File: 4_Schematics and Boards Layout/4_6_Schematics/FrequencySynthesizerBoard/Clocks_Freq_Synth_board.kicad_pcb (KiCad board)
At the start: 6 copper layers, 100 x 100 mm, 188 parts, among them IC1 AD9523BCPZ, J1 142-0731-211, J10 142-0731-211, J11 142-0731-211, J12 142-0731-211, J13 142-0731-211, J2 142-0731-211, J3 CJT-T-P-HH-ST-TH1, J4 CJT-T-P-HH-ST-TH1, J5 142-0731-211, J6 142-0731-211, J7 142-0731-211, J8 142-0731-211, J9 142-0731-211, U1 ADF4382ABCCZ, U10 ATS1005-3DB-FD-T05, U2 MTX2-143+, U3 MTX2-143+, U4 ATS1005-3DB-FD-T05, U5 ATS1005-3DB-FD-T05, U6 ADF4382ABCCZ, U7 MTX2-143+, U8 ATS1005-3DB-FD-T05, U9 MTX2-143+, X10 22-23-2021, X11 22-23-2021, X12 22-23-2021, X13 22-23-2021, X14 22-23-2021, X15 22-23-2021, X4 ECOC-2522-100.000-3HC, X5 CVHD-950-50.000, X6 CVHD-950-50.000

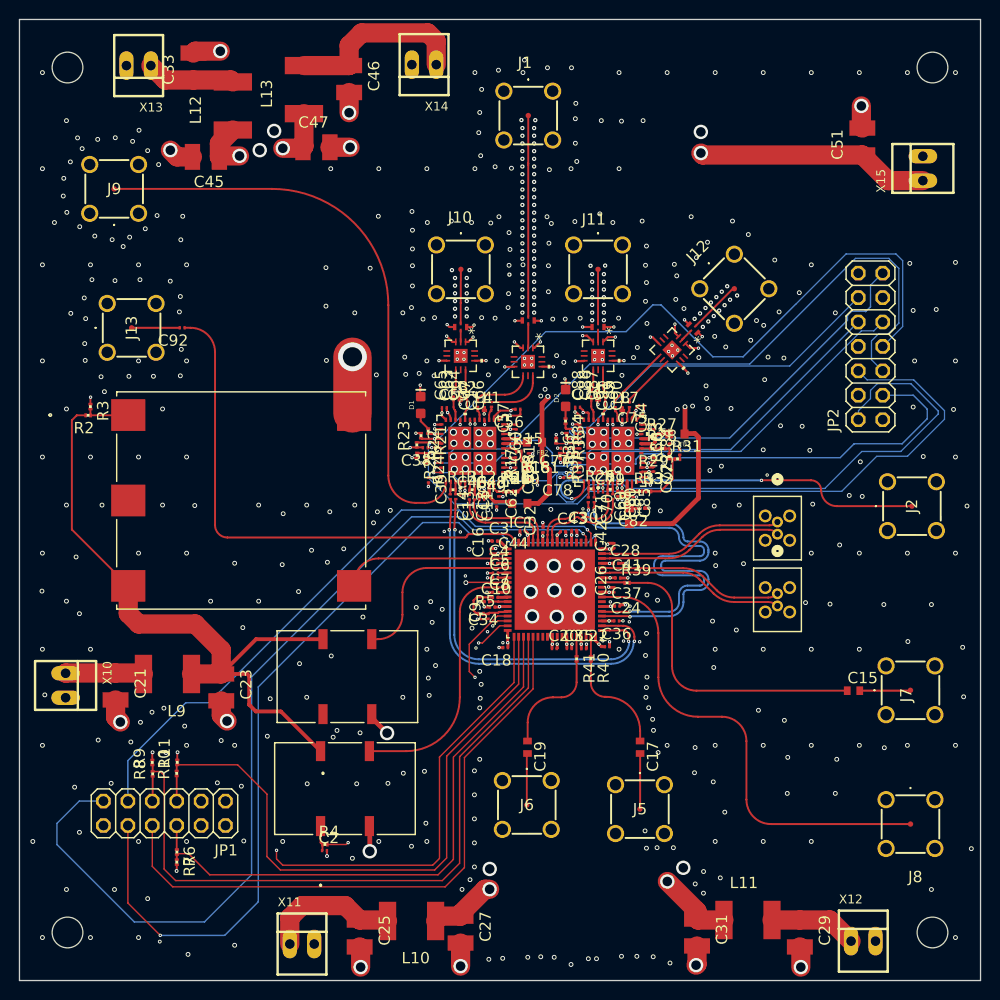
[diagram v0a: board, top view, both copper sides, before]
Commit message: Add freq synth board: schematic, gerbers, drills, BOM, DRC-fixed PCB
Includes:
- Restored schematic (.kicad_sch) from Eagle import history
- Sub-schematic sheet (_1.kicad_sch)
- Eagle import symbol library (.kicad_sym)
- JLCPCB 6-layer gerber set (F/B/In1-4 Cu, masks, paste, silkscreen)
- PTH + NPTH drill files with drill map PDF
- JLCPCB BOM (.xls) and component placement (.csv)
- Updated PCB with via clearance + upsize fixes (1508 -> 661 DRC violations)
- Updated project file with JLCPCB design rules
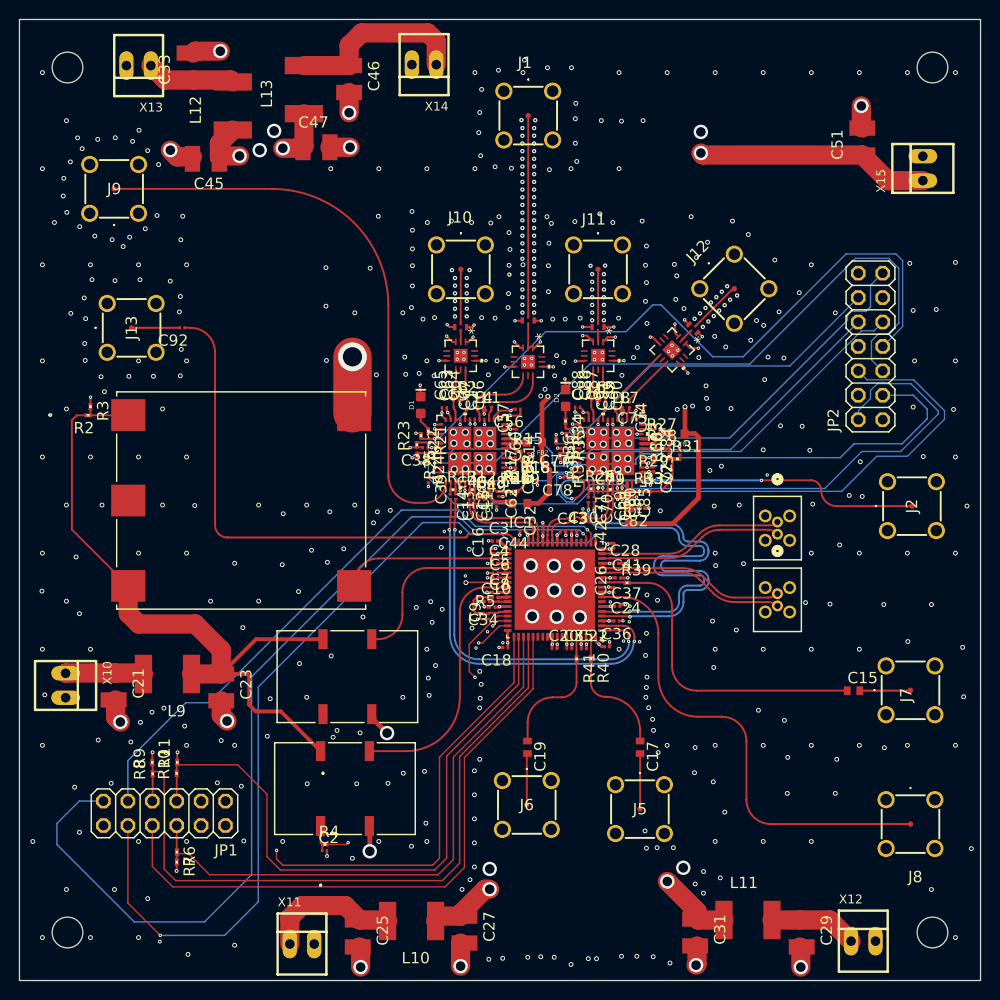
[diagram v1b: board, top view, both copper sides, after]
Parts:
- moved C33 0.40 mm to (116.2, 59.9)
- moved C27 0.40 mm to (144.8, 149.7)
- moved C25 0.20 mm to (133.7, 150.1)
- moved C29 0.20 mm to (179.9, 150.1)
- moved C31 0.20 mm to (168.8, 150.0)
- moved C45 0.20 mm to (117.9, 69.5)
- moved C21 0.20 mm to (108.3, 124.4)
